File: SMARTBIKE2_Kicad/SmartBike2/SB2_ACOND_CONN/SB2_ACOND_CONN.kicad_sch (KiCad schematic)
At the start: 0 parts

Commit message: Fase 2 de 3 panel full
+ PCB Acondicionamiento y Módulos

~ Esquemático Luces
~ PCB 3 de 3, Luces
~ Panelización
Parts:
- added H1, H2: MountingHole, MountingHole:MountingHole_2.2mm_M2, symbol Mechanical:MountingHole
- added J1: Conn_01x02, Connector_JST:JST_EH_B2B-EH-A_1x02_P2.50mm_Vertical, symbol Connector_Generic:Conn_01x02
- added J2: Conn_01x01, Connector_PinHeader_1.00mm:PinHeader_1x01_P1.00mm_Vertical, symbol Connector_Generic:Conn_01x01
- added JH1: ~, Connector_JST:JST_EH_B8B-EH-A_1x08_P2.50mm_Vertical, symbol Power_Conn_01x02:Hybrid_Conn_01x08_53
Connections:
- new net +3.3V: JH1.4
- new net +3.3_2: JH1.3
- new net 4.1V: JH1.1
- new net Acondicionamiento/CtrAl: JH1.8
- new net Acondicionamiento/CtrGPSAc: JH1.6
- new net Acondicionamiento/CtrLuces: J1.1 (Pin_1)
- new net Acondicionamiento/CtrSIM: JH1.7
- new net GND: J1.2 (Pin_2), JH1.2, JH1.5
- new net VdoSIM: J2.1 (Pin_1)
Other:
- sheet Acondicionamiento ports: added CtrAl, CtrGPSAc, CtrLuces, CtrSIM, NE_SIM, RST_SIM, RX_GPS, RX_SIM, SCL, SDA, TX_GPS, TX_SIM; removed none
- sheet Conectores_Modulos ports: added NE, RstSIM, RxGPS, RxSIM, TxGPS, TxSIM, VDO_SIM, mSCL, mSDA; removed none
- note added: "Comunicación con la alimentación. Potencia."
- note added: "Control Luces"

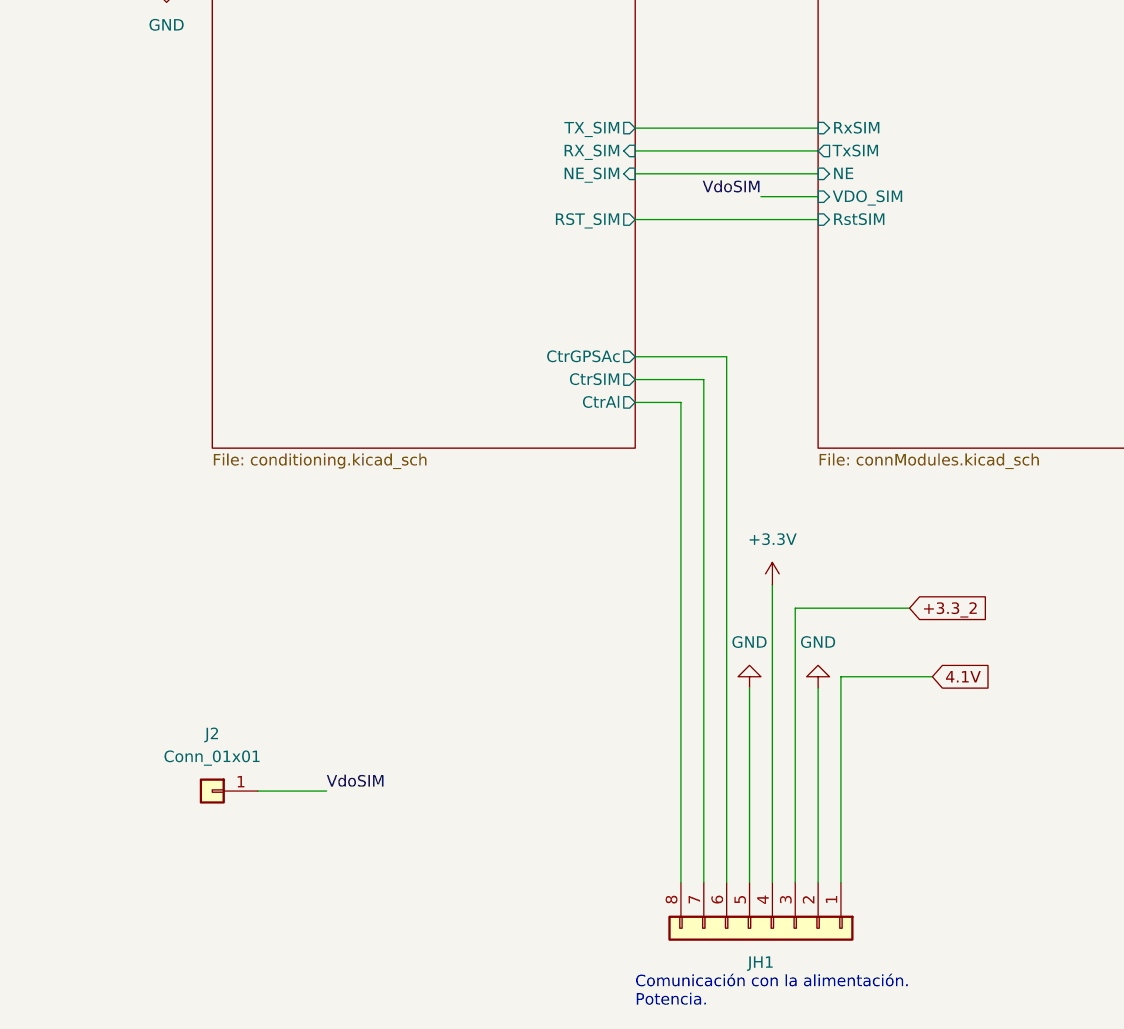
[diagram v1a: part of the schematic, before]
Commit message: Impresión vías sin metalización
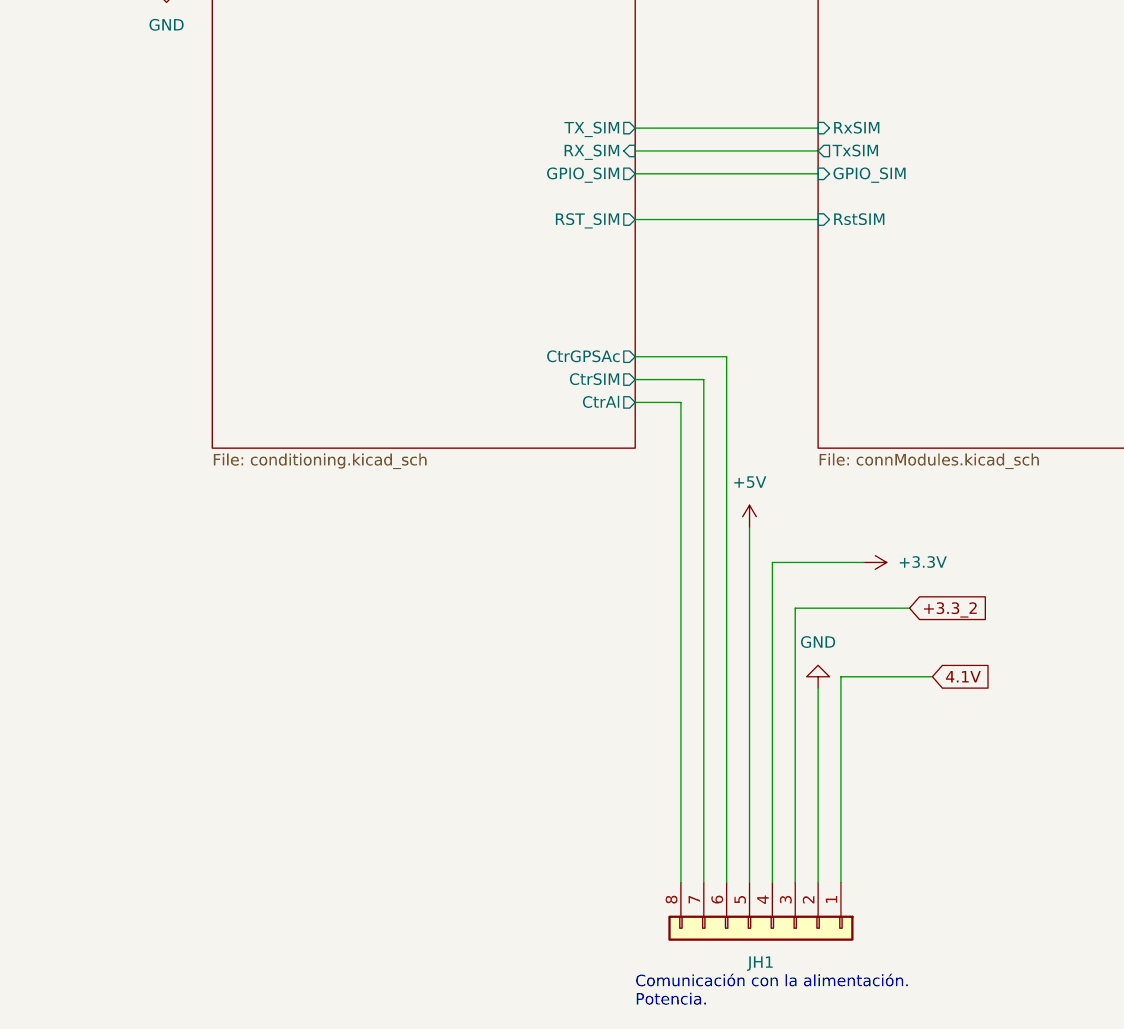
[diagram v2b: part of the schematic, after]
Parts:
- removed J2: Conn_01x01, Connector_PinHeader_1.00mm:PinHeader_1x01_P1.00mm_Vertical, symbol Connector_Generic:Conn_01x01
- JH1: footprint Connector_JST:JST_EH_B8B-EH-A_1x08_P2.50mm_Vertical -> Connector_JST:JST_XH_B8B-XH-A_1x08_P2.50mm_Vertical
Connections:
- net GND: no longer JH1.5
- new net +5V: JH1.5
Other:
- sheet Acondicionamiento ports: added GPIO_SIM; removed NE_SIM
- sheet Conectores_Modulos ports: added GPIO_SIM; removed NE, VDO_SIM
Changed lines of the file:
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@@
     (stroke (width 0) (type default))
   )
-  (wire (pts (xy 104.14 123.19) (xy 104.14 156.21))
-    (stroke (width 0) (type default))
-  )
-  (wire (pts (xy 102.87 80.01) (xy 109.22 80.01))
+  (wire (pts (xy 104.14 120.65) (xy 104.14 156.21))
     (stroke (width 0) (type default))
   )
@@
     (stroke (width 0) (type default))
   )
-  (wire (pts (xy 46.99 146.05) (xy 54.61 146.05))
-    (stroke (width 0) (type default))
-  )
-  (wire (pts (xy 101.6 134.62) (xy 101.6 156.21))
+  (wire (pts (xy 104.14 120.65) (xy 114.3 120.65))
+    (stroke (width 0) (type default))
+  )
+  (wire (pts (xy 101.6 116.84) (xy 101.6 156.21))
     (stroke (width 0) (type default))
   )
@@
   (text "Comunicación con la alimentación.\nPotencia.\n" (at 88.9 170.18 0)
     (effects (font (size 1.27 1.27)) (justify left bottom))
-  )
-  (label "VdoSIM" (at 54.61 146.05 0) (fields_autoplaced)
-    (effects (font (size 1.27 1.27)) (justify left bottom))
-  )
-  (label "VdoSIM" (at 102.87 80.01 180) (fields_autoplaced)
-    (effects (font (size 1.27 1.27)) (justify right bottom))
   )
   (global_label "4.1V" (shape input) (at 121.92 133.35 0) (fields_autoplaced)
@@
     )
   )
-  (symbol (lib_id "power:GND") (at 101.6 134.62 180) (unit 1)
-    (in_bom yes) (on_board yes) (dnp no) (fields_autoplaced)
-    (property "Reference" "#PWR02" (at 101.6 128.27 0)
-      (effects (font (size 1.27 1.27)) hide)
-    )
-    (property "Value" "GND" (at 101.6 129.54 0)
-      (effects (font (size 1.27 1.27)))
-    )
-    (property "Footprint" "" (at 101.6 134.62 0)
-      (effects (font (size 1.27 1.27)) hide)
-    )
-    (property "Datasheet" "" (at 101.6 134.62 0)
-      (effects (font (size 1.27 1.27)) hide)
-    )
-    (pin "1")
-    (instances
-      (project "SB2_ACOND_CONN"
-        (path "/f851423c-110f-48a5-8b48-ed3566b6f957"
-          (reference "#PWR02") (unit 1)
-        )
-      )
-    )
-  )
   (symbol (lib_id "Mechanical:MountingHole") (at 220.98 41.91 0) (unit 1)
     (in_bom yes) (on_board yes) (dnp no) (fields_autoplaced)
@@
     )
   )
+  (symbol (lib_id "power:+3.3V") (at 114.3 120.65 270) (unit 1)
+    (in_bom yes) (on_board yes) (dnp no) (fields_autoplaced)
+    (property "Reference" "#PWR04" (at 110.49 120.65 0)
+      (effects (font (size 1.27 1.27)) hide)
+    )
+    (property "Value" "+3.3V" (at 118.11 120.65 90)
+      (effects (font (size 1.27 1.27)) (justify left))
+    )
+    (property "Footprint" "" (at 114.3 120.65 0)
+      (effects (font (size 1.27 1.27)) hide)
+    )
+    (property "Datasheet" "" (at 114.3 120.65 0)
+      (effects (font (size 1.27 1.27)) hide)
+    )
+    (pin "1")
+    (instances
+      (project "SB2_ACOND_CONN"
+        (path "/f851423c-110f-48a5-8b48-ed3566b6f957"
+          (reference "#PWR04") (unit 1)
+        )
+      )
+    )
+  )
   (symbol (lib_id "Power_Conn_01x02:Hybrid_Conn_01x08_53") (at 96.52 156.21 270) (unit 1)
     (in_bom yes) (on_board yes) (dnp no) (fields_autoplaced)
@@
       (effects (font (size 1.27 1.27)))
     )
-    (property "Footprint" "Connector_JST:JST_EH_B8B-EH-A_1x08_P2.50mm_Vertical" (at 96.52 156.21 0)
+    (property "Footprint" "Connector_JST:JST_XH_B8B-XH-A_1x08_P2.50mm_Vertical" (at 96.52 156.21 0)
       (effects (font (size 1.27 1.27)) hide)
     )
@@
       (effects (font (size 1.27 1.27)) hide)
     )
-    (pin "8")
-    (pin "1")
+    (pin "4")
+    (pin "5")
+    (pin "7")
+    (pin "2")
     (pin "3")
     (pin "6")
-    (pin "5")
+    (pin "8")
+    (pin "1")
+    (instances
+      (project "SB2_ACOND_CONN"
+        (path "/f851423c-110f-48a5-8b48-ed3566b6f957"
+          (reference "JH1") (unit 1)
+        )
+      )
+    )
+  )
+  (symbol (lib_id "power:+5V") (at 101.6 116.84 0) (unit 1)
+    (in_bom yes) (on_board yes) (dnp no) (fields_autoplaced)
+    (property "Reference" "#PWR02" (at 101.6 120.65 0)
+      (effects (font (size 1.27 1.27)) hide)
+    )
+    (property "Value" "+5V" (at 101.6 111.76 0)
+      (effects (font (size 1.27 1.27)))
+    )
+    (property "Footprint" "" (at 101.6 116.84 0)
+      (effects (font (size 1.27 1.27)) hide)
+    )
+    (property "Datasheet" "" (at 101.6 116.84 0)
+      (effects (font (size 1.27 1.27)) hide)
+    )
+    (pin "1")
+    (instances
+      (project "SB2_ACOND_CONN"
+        (path "/f851423c-110f-48a5-8b48-ed3566b6f957"
+          (reference "#PWR02") (unit 1)
+        )
+      )
+    )
+  )
+  (symbol (lib_id "power:GND") (at 109.22 134.62 180) (unit 1)
+    (in_bom yes) (on_board yes) (dnp no) (fields_autoplaced)
+    (property "Reference" "#PWR03" (at 109.22 128.27 0)
+      (effects (font (size 1.27 1.27)) hide)
+    )
+    (property "Value" "GND" (at 109.22 129.54 0)
+      (effects (font (size 1.27 1.27)))
+    )
+    (property "Footprint" "" (at 109.22 134.62 0)
+      (effects (font (size 1.27 1.27)) hide)
+    )
+    (property "Datasheet" "" (at 109.22 134.62 0)
+      (effects (font (size 1.27 1.27)) hide)
+    )
+    (pin "1")
+    (instances
+      (project "SB2_ACOND_CONN"
+        (path "/f851423c-110f-48a5-8b48-ed3566b6f957"
+          (reference "#PWR03") (unit 1)
+        )
+      )
+    )
+  )
+  (symbol (lib_id "Connector_Generic:Conn_01x02") (at 27.94 48.26 0) (mirror y) (unit 1)
+    (in_bom yes) (on_board yes) (dnp no) (fields_autoplaced)
+    (property "Reference" "J1" (at 27.94 41.91 0)
+      (effects (font (size 1.27 1.27)))
+    )
+    (property "Value" "Conn_01x02" (at 27.94 44.45 0)
+      (effects (font (size 1.27 1.27)))
+    )
+    (property "Footprint" "Connector_JST:JST_EH_B2B-EH-A_1x02_P2.50mm_Vertical" (at 27.94 48.26 0)
+      (effects (font (size 1.27 1.27)) hide)
+    )
+    (property "Datasheet" "~" (at 27.94 48.26 0)
+      (effects (font (size 1.27 1.27)) hide)
+    )
+    (pin "1")
     (pin "2")
-    (pin "7")
-    (pin "4")
-    (instances
-      (project "SB2_ACOND_CONN"
-        (path "/f851423c-110f-48a5-8b48-ed3566b6f957"
-          (reference "JH1") (unit 1)
-        )
-      )
-    )
-  )
-  (symbol (lib_id "power:+3.3V") (at 104.14 123.19 0) (unit 1)
-    (in_bom yes) (on_board yes) (dnp no) (fields_autoplaced)
-    (property "Reference" "#PWR03" (at 104.14 127 0)
-      (effects (font (size 1.27 1.27)) hide)
-    )
-    (property "Value" "+3.3V" (at 104.14 118.11 0)
-      (effects (font (size 1.27 1.27)))
-    )
-    (property "Footprint" "" (at 104.14 123.19 0)
-      (effects (font (size 1.27 1.27)) hide)
-    )
-    (property "Datasheet" "" (at 104.14 123.19 0)
-      (effects (font (size 1.27 1.27)) hide)
-    )
-    (pin "1")
-    (instances
-      (project "SB2_ACOND_CONN"
-        (path "/f851423c-110f-48a5-8b48-ed3566b6f957"
-          (reference "#PWR03") (unit 1)
-        )
-      )
-    )
-  )
-  (symbol (lib_id "power:GND") (at 109.22 134.62 180) (unit 1)
-    (in_bom yes) (on_board yes) (dnp no) (fields_autoplaced)
-    (property "Reference" "#PWR04" (at 109.22 128.27 0)
-      (effects (font (size 1.27 1.27)) hide)
-    )
-    (property "Value" "GND" (at 109.22 129.54 0)
-      (effects (font (size 1.27 1.27)))
-    )
-    (property "Footprint" "" (at 109.22 134.62 0)
-      (effects (font (size 1.27 1.27)) hide)
-    )
-    (property "Datasheet" "" (at 109.22 134.62 0)
-      (effects (font (size 1.27 1.27)) hide)
-    )
-    (pin "1")
-    (instances
-      (project "SB2_ACOND_CONN"
-        (path "/f851423c-110f-48a5-8b48-ed3566b6f957"
-          (reference "#PWR04") (unit 1)
-        )
-      )
-    )
-  )
-  (symbol (lib_id "Connector_Generic:Conn_01x02") (at 27.94 48.26 0) (mirror y) (unit 1)
-    (in_bom yes) (on_board yes) (dnp no) (fields_autoplaced)
-    (property "Reference" "J1" (at 27.94 41.91 0)
-      (effects (font (size 1.27 1.27)))
-    )
-    (property "Value" "Conn_01x02" (at 27.94 44.45 0)
-      (effects (font (size 1.27 1.27)))
-    )
-    (property "Footprint" "Connector_JST:JST_EH_B2B-EH-A_1x02_P2.50mm_Vertical" (at 27.94 48.26 0)
-      (effects (font (size 1.27 1.27)) hide)
-    )
-    (property "Datasheet" "~" (at 27.94 48.26 0)
-      (effects (font (size 1.27 1.27)) hide)
-    )
-    (pin "1")
-    (pin "2")
     (instances
       (project "SB2_ACOND_CONN"
         (path "/f851423c-110f-48a5-8b48-ed3566b6f957"
           (reference "J1") (unit 1)
-        )
-      )
-    )
-  )
-  (symbol (lib_id "Connector_Generic:Conn_01x01") (at 41.91 146.05 0) (mirror y) (unit 1)
-    (in_bom yes) (on_board yes) (dnp no) (fields_autoplaced)
-    (property "Reference" "J2" (at 41.91 139.7 0)
-      (effects (font (size 1.27 1.27)))
-    )
-    (property "Value" "Conn_01x01" (at 41.91 142.24 0)
-      (effects (font (size 1.27 1.27)))
-    )
-    (property "Footprint" "Connector_PinHeader_1.00mm:PinHeader_1x01_P1.00mm_Vertical" (at 41.91 146.05 0)
-      (effects (font (size 1.27 1.27)) hide)
-    )
-    (property "Datasheet" "~" (at 41.91 146.05 0)
-      (effects (font (size 1.27 1.27)) hide)
-    )
-    (pin "1")
-    (instances
-      (project "SB2_ACOND_CONN"
-        (path "/f851423c-110f-48a5-8b48-ed3566b6f957"
-          (reference "J2") (unit 1)
         )
       )
@@
       (effects (font (size 1.27 1.27)) (justify left))
     )
-    (pin "NE" input (at 109.22 77.47 180)
-      (effects (font (size 1.27 1.27)) (justify left))
-    )
     (pin "RstSIM" input (at 109.22 82.55 180)
       (effects (font (size 1.27 1.27)) (justify left))
     )
-    (pin "VDO_SIM" input (at 109.22 80.01 180)
+    (pin "GPIO_SIM" input (at 109.22 77.47 180)
       (effects (font (size 1.27 1.27)) (justify left))
     )
@@
       (effects (font (size 1.27 1.27)) (justify right))
     )
-    (pin "NE_SIM" input (at 88.9 77.47 0)
-      (effects (font (size 1.27 1.27)) (justify right))
-    )
     (pin "RST_SIM" output (at 88.9 82.55 0)
       (effects (font (size 1.27 1.27)) (justify right))
@@
       (effects (font (size 1.27 1.27)) (justify left))
     )
-    (instances
+    (pin "GPIO_SIM" output (at 88.9 77.47 0)
+      (effects (font (size 1.27 1.27)) (justify right))
+    )
+    (instances
